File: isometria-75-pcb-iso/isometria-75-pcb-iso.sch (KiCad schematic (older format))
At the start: 32 parts, among them J101 USB, J102 SPI, J103 Conn_01x01_Male, Q101 AO3400A, SW101 RST, SW102 BOOT, U101 XC6206P332MR, U102 STM32F072CBTx

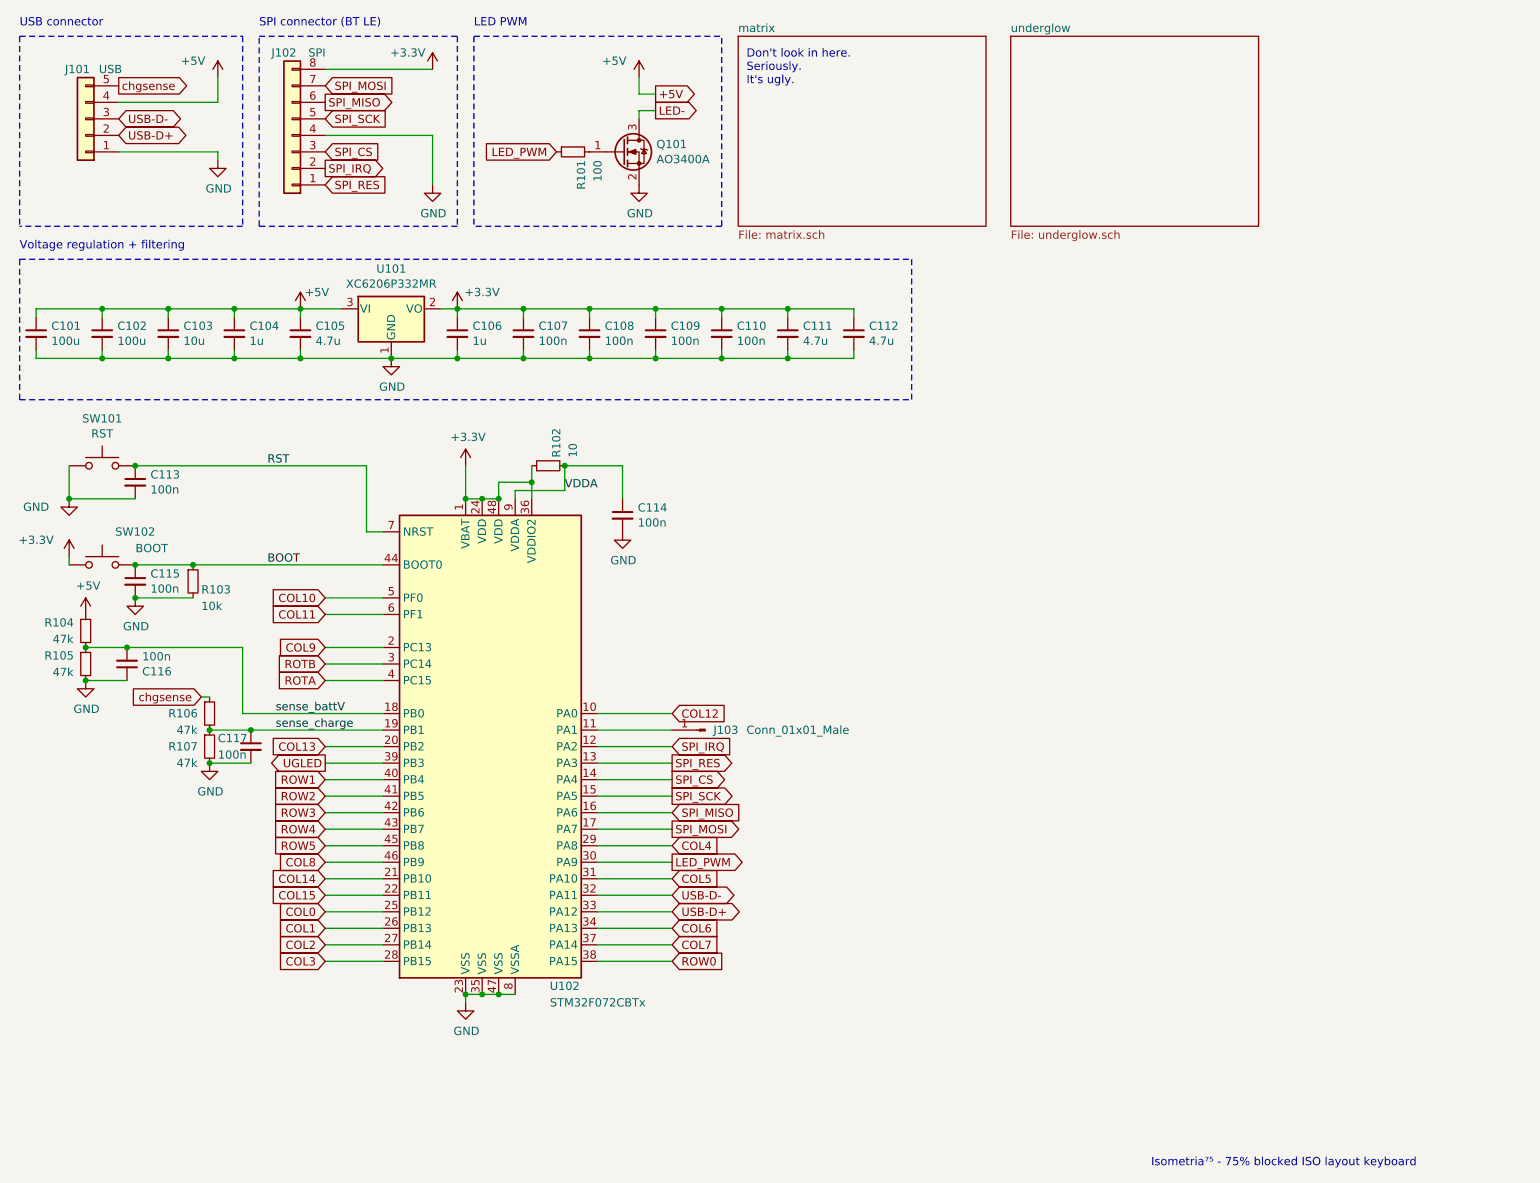
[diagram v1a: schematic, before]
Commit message: improved componend value formatting
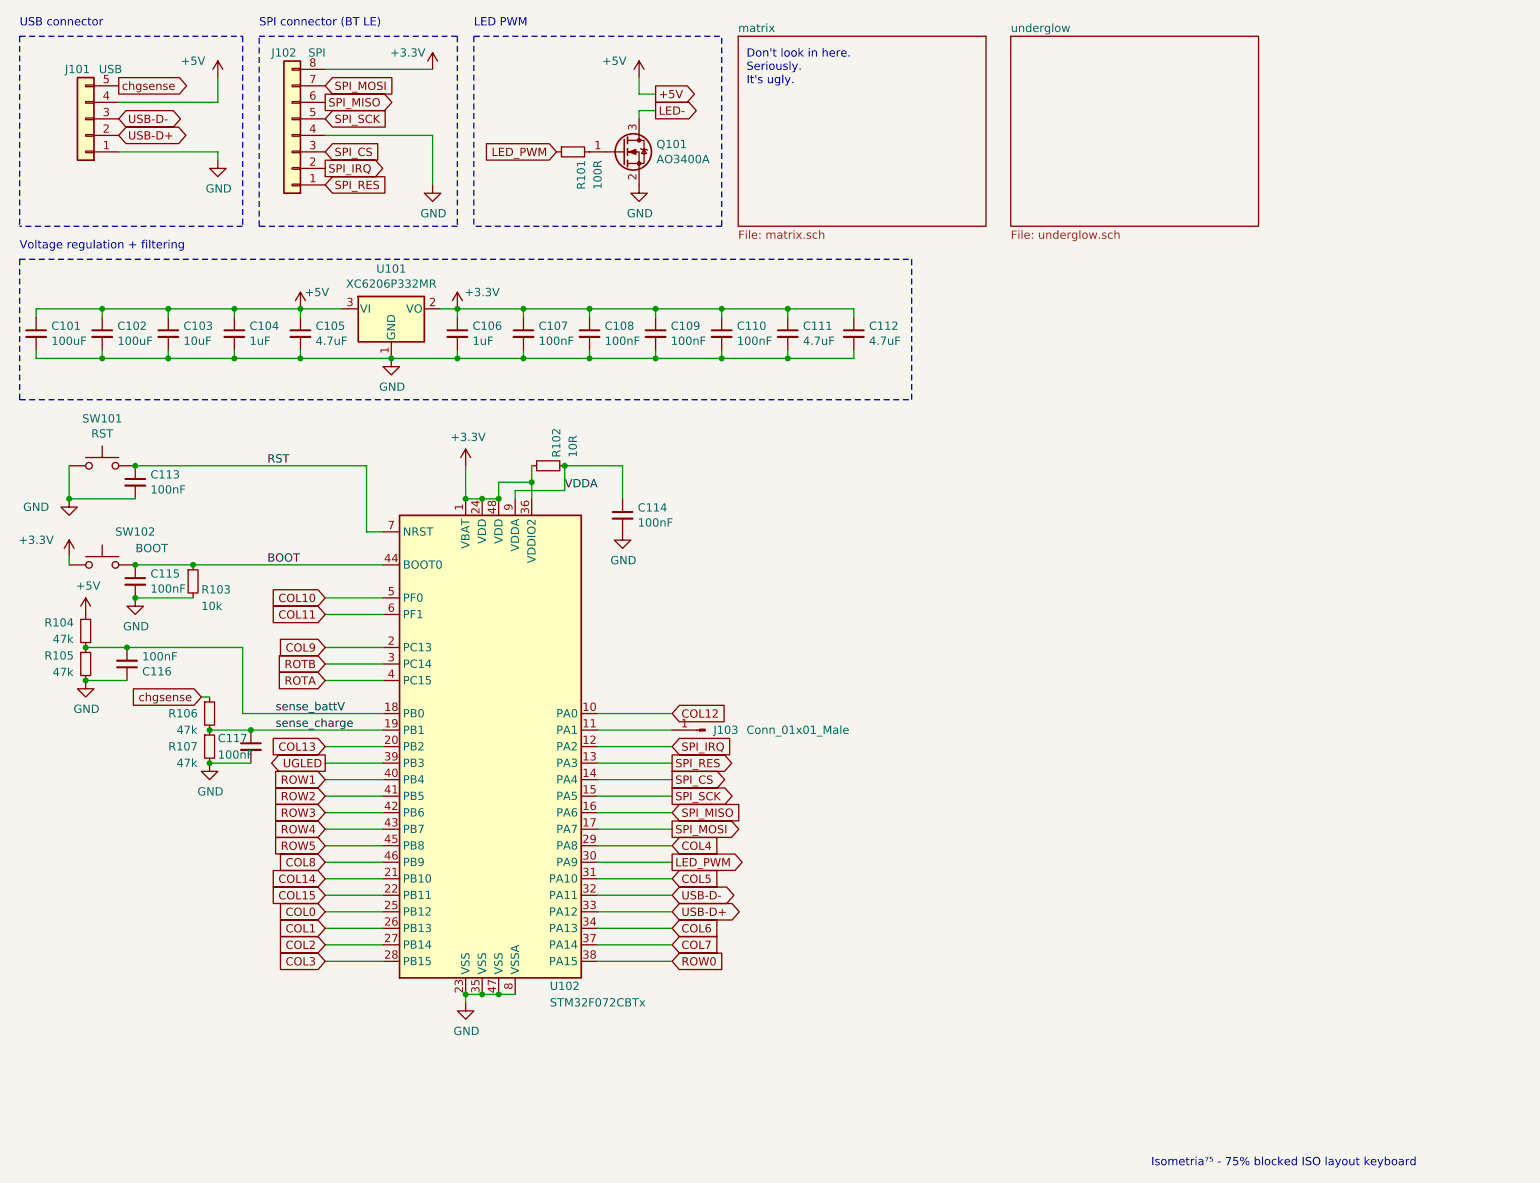
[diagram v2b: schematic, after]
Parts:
- C101, C102: value 100u -> 100uF
- C103: value 10u -> 10uF
- C104, C106: value 1u -> 1uF
- C105, C111, C112: value 4.7u -> 4.7uF
- C107, C108, C109, C110, C113, C114, C115, C116, C117: value 100n -> 100nF
- J101, J102, J103: LCSC / -> (none)
- R101: value 100 -> 100R
- R102: value 10 -> 10R
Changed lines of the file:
@@
 P 4200 3550
 F 0 "C114" H 4292 3596 50  0000 L CNN
-F 1 "100n" H 4292 3505 50  0000 L CNN
+F 1 "100nF" H 4292 3505 50  0000 L CNN
 F 2 "Capacitor_SMD:C_0402_1005Metric" H 4200 3550 50  0001 C CNN
 F 3 "~" H 4200 3550 50  0001 C CNN
@@
 P 1250 3350
 F 0 "C113" H 1342 3396 50  0000 L CNN
-F 1 "100n" H 1342 3305 50  0000 L CNN
+F 1 "100nF" H 1342 3305 50  0000 L CNN
 F 2 "Capacitor_SMD:C_0402_1005Metric" H 1250 3350 50  0001 C CNN
 F 3 "~" H 1250 3350 50  0001 C CNN
@@
 P 3750 3250
 F 0 "R102" H 3800 3200 50  0000 L CNN
-F 1 "10" H 3800 3100 50  0000 L CNN
+F 1 "10R" H 3800 3100 50  0000 L CNN
 F 2 "Resistor_SMD:R_0402_1005Metric" H 3750 3250 50  0001 C CNN
 F 3 "~" H 3750 3250 50  0001 C CNN
@@
 P 1950 4950
 F 0 "C117" H 1750 5000 50  0000 L CNN
-F 1 "100n" H 1750 4900 50  0000 L CNN
+F 1 "100nF" H 1750 4900 50  0000 L CNN
 F 2 "Capacitor_SMD:C_0402_1005Metric" H 1950 4950 50  0001 C CNN
 F 3 "~" H 1950 4950 50  0001 C CNN
@@
 P 3900 1350
 F 0 "R101" H 3950 1300 50  0000 L CNN
-F 1 "100" H 3950 1200 50  0000 L CNN
+F 1 "100R" H 3950 1200 50  0000 L CNN
 F 2 "Resistor_SMD:R_0402_1005Metric" H 3900 1350 50  0001 C CNN
 F 3 "~" H 3900 1350 50  0001 C CNN
@@
 F 2 "Connector_JST:JST_SH_SM05B-SRSS-TB_1x05-1MP_P1.00mm_Horizontal" H 950 1150 50  0001 C CNN
 F 3 "http://www.jst-mfg.com/product/pdf/eng/ePH.pdf" H 950 1150 50  0001 C CNN
-F 4 "/" H 950 1150 50  0001 C CNN "LCSC"
+F 4 "" H 950 1150 50  0001 C CNN "LCSC"
 	1    950  1150
 	-1   0    0    1
@@
 P 3200 2450
 F 0 "C106" H 3292 2496 50  0000 L CNN
-F 1 "1u" H 3292 2405 50  0000 L CNN
+F 1 "1uF" H 3292 2405 50  0000 L CNN
 F 2 "Capacitor_SMD:C_0402_1005Metric" H 3200 2450 50  0001 C CNN
 F 3 "~" H 3200 2450 50  0001 C CNN
@@
 P 1850 2450
 F 0 "C104" H 1942 2496 50  0000 L CNN
-F 1 "1u" H 1942 2405 50  0000 L CNN
+F 1 "1uF" H 1942 2405 50  0000 L CNN
 F 2 "Capacitor_SMD:C_0402_1005Metric" H 1850 2450 50  0001 C CNN
 F 3 "~" H 1850 2450 50  0001 C CNN
@@
 P 5200 2450
 F 0 "C111" H 5292 2496 50  0000 L CNN
-F 1 "4.7u" H 5292 2405 50  0000 L CNN
+F 1 "4.7uF" H 5292 2405 50  0000 L CNN
 F 2 "Capacitor_SMD:C_0402_1005Metric" H 5200 2450 50  0001 C CNN
 F 3 "~" H 5200 2450 50  0001 C CNN
@@
 P 4800 2450
 F 0 "C110" H 4892 2496 50  0000 L CNN
-F 1 "100n" H 4892 2405 50  0000 L CNN
+F 1 "100nF" H 4892 2405 50  0000 L CNN
 F 2 "Capacitor_SMD:C_0402_1005Metric" H 4800 2450 50  0001 C CNN
 F 3 "~" H 4800 2450 50  0001 C CNN
@@
 P 4400 2450
 F 0 "C109" H 4492 2496 50  0000 L CNN
-F 1 "100n" H 4492 2405 50  0000 L CNN
+F 1 "100nF" H 4492 2405 50  0000 L CNN
 F 2 "Capacitor_SMD:C_0402_1005Metric" H 4400 2450 50  0001 C CNN
 F 3 "~" H 4400 2450 50  0001 C CNN
@@
 P 4000 2450
 F 0 "C108" H 4092 2496 50  0000 L CNN
-F 1 "100n" H 4092 2405 50  0000 L CNN
+F 1 "100nF" H 4092 2405 50  0000 L CNN
 F 2 "Capacitor_SMD:C_0402_1005Metric" H 4000 2450 50  0001 C CNN
 F 3 "~" H 4000 2450 50  0001 C CNN
@@
 P 3600 2450
 F 0 "C107" H 3692 2496 50  0000 L CNN
-F 1 "100n" H 3692 2405 50  0000 L CNN
+F 1 "100nF" H 3692 2405 50  0000 L CNN
 F 2 "Capacitor_SMD:C_0402_1005Metric" H 3600 2450 50  0001 C CNN
 F 3 "~" H 3600 2450 50  0001 C CNN
@@
 P 2250 2450
 F 0 "C105" H 2342 2496 50  0000 L CNN
-F 1 "4.7u" H 2342 2405 50  0000 L CNN
+F 1 "4.7uF" H 2342 2405 50  0000 L CNN
 F 2 "Capacitor_SMD:C_0402_1005Metric" H 2250 2450 50  0001 C CNN
 F 3 "~" H 2250 2450 50  0001 C CNN
@@
 P 5600 2450
 F 0 "C112" H 5692 2496 50  0000 L CNN
-F 1 "4.7u" H 5692 2405 50  0000 L CNN
+F 1 "4.7uF" H 5692 2405 50  0000 L CNN
 F 2 "Capacitor_SMD:C_0402_1005Metric" H 5600 2450 50  0001 C CNN
 F 3 "~" H 5600 2450 50  0001 C CNN
@@
 P 1250 3950
 F 0 "C115" H 1342 3996 50  0000 L CNN
-F 1 "100n" H 1342 3905 50  0000 L CNN
+F 1 "100nF" H 1342 3905 50  0000 L CNN
 F 2 "Capacitor_SMD:C_0402_1005Metric" H 1250 3950 50  0001 C CNN
 F 3 "~" H 1250 3950 50  0001 C CNN
@@
 F 2 "Connector_JST:JST_SH_SM08B-SRSS-TB_1x08-1MP_P1.00mm_Horizontal" H 2200 1250 50  0001 C CNN
 F 3 "~" H 2200 1250 50  0001 C CNN
-F 4 "/" H 2200 1250 50  0001 C CNN "LCSC"
+F 4 "" H 2200 1250 50  0001 C CNN "LCSC"
 	1    2200 1250
 	-1   0    0    1
@@
 P 1200 4450
 F 0 "C116" H 1292 4496 50  0000 L CNN
-F 1 "100n" H 1292 4405 50  0000 L CNN
+F 1 "100nF" H 1292 4405 50  0000 L CNN
 F 2 "Capacitor_SMD:C_0402_1005Metric" H 1200 4450 50  0001 C CNN
 F 3 "~" H 1200 4450 50  0001 C CNN
@@
 P 1450 2450
 F 0 "C103" H 1542 2496 50  0000 L CNN
-F 1 "10u" H 1542 2405 50  0000 L CNN
+F 1 "10uF" H 1542 2405 50  0000 L CNN
 F 2 "Capacitor_Tantalum_SMD:CP_EIA-3216-18_Kemet-A" H 1450 2450 50  0001 C CNN
 F 3 "~" H 1450 2450 50  0001 C CNN
@@
 P 1050 2450
 F 0 "C102" H 1142 2496 50  0000 L CNN
-F 1 "100u" H 1142 2405 50  0000 L CNN
+F 1 "100uF" H 1142 2405 50  0000 L CNN
 F 2 "Capacitor_Tantalum_SMD:CP_EIA-3528-21_Kemet-B" H 1050 2450 50  0001 C CNN
 F 3 "~" H 1050 2450 50  0001 C CNN
@@
 P 650 2450
 F 0 "C101" H 742 2496 50  0000 L CNN
-F 1 "100u" H 742 2405 50  0000 L CNN
+F 1 "100uF" H 742 2405 50  0000 L CNN
 F 2 "Capacitor_Tantalum_SMD:CP_EIA-3528-21_Kemet-B" H 650 2450 50  0001 C CNN
 F 3 "~" H 650 2450 50  0001 C CNN
@@
 F 2 "Connector_PinHeader_2.54mm:PinHeader_1x01_P2.54mm_Vertical" H 4700 4850 50  0001 C CNN
 F 3 "~" H 4700 4850 50  0001 C CNN
-F 4 "/" H 4700 4850 50  0001 C CNN "LCSC"
+F 4 "" H 4700 4850 50  0001 C CNN "LCSC"
 	1    4700 4850
 	-1   0    0    1
